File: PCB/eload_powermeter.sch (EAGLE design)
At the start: 66 parts, among them IC1 ADS1115_IC, IC2 AD826R, IC3 TP4056, IC4 FS312F-G, IC5 MT3608, K1 HJR-4102E, K2 TXD2SA-4.5V, Q1 BSS123, Q2 YSX321SL20H, Q3 BSS123, Q4 IRF520, Q5 BSS123, SW1 ENCODER, U1 ATMEGA328P-AU

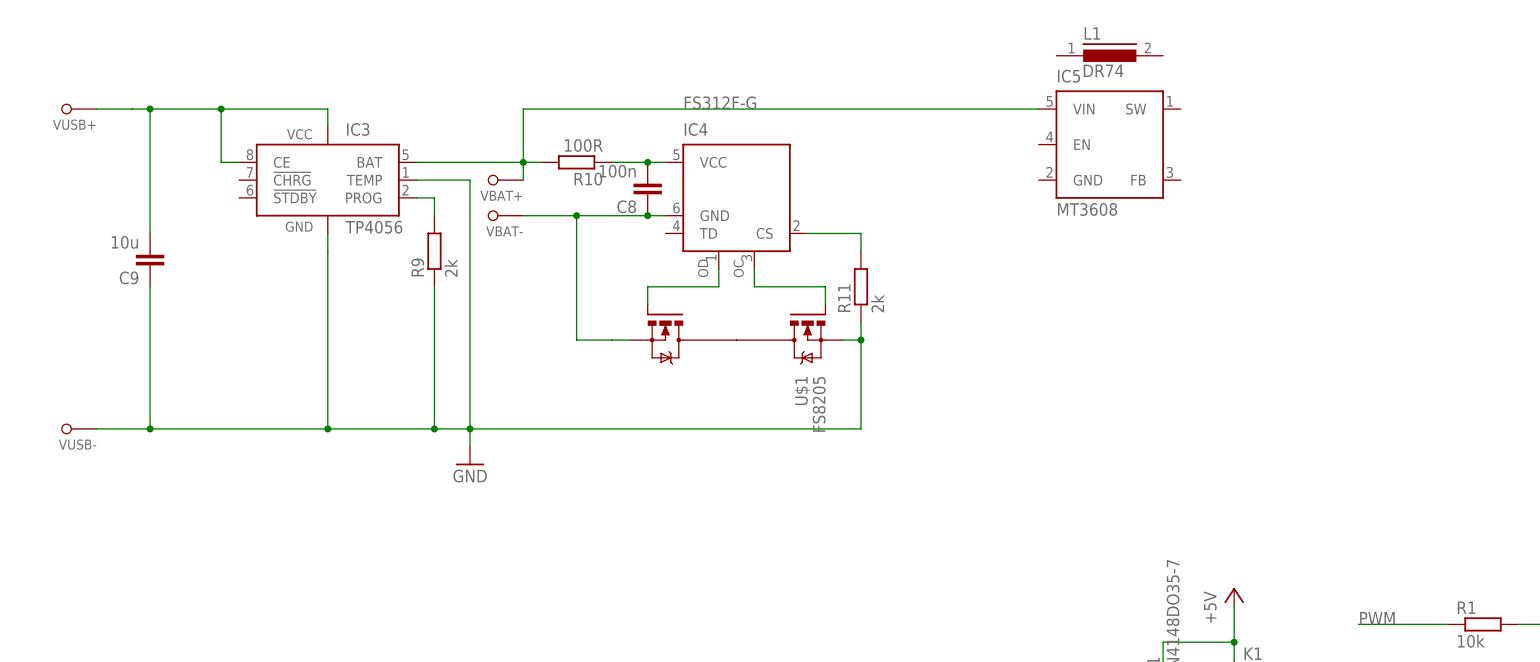
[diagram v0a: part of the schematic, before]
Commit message: finish boost circuit, start reverse surface mount led
Finishing the boost converter circuit and selecting the inductor and the schottky diode.
Starting with the footprint of the reverse surface mount led.
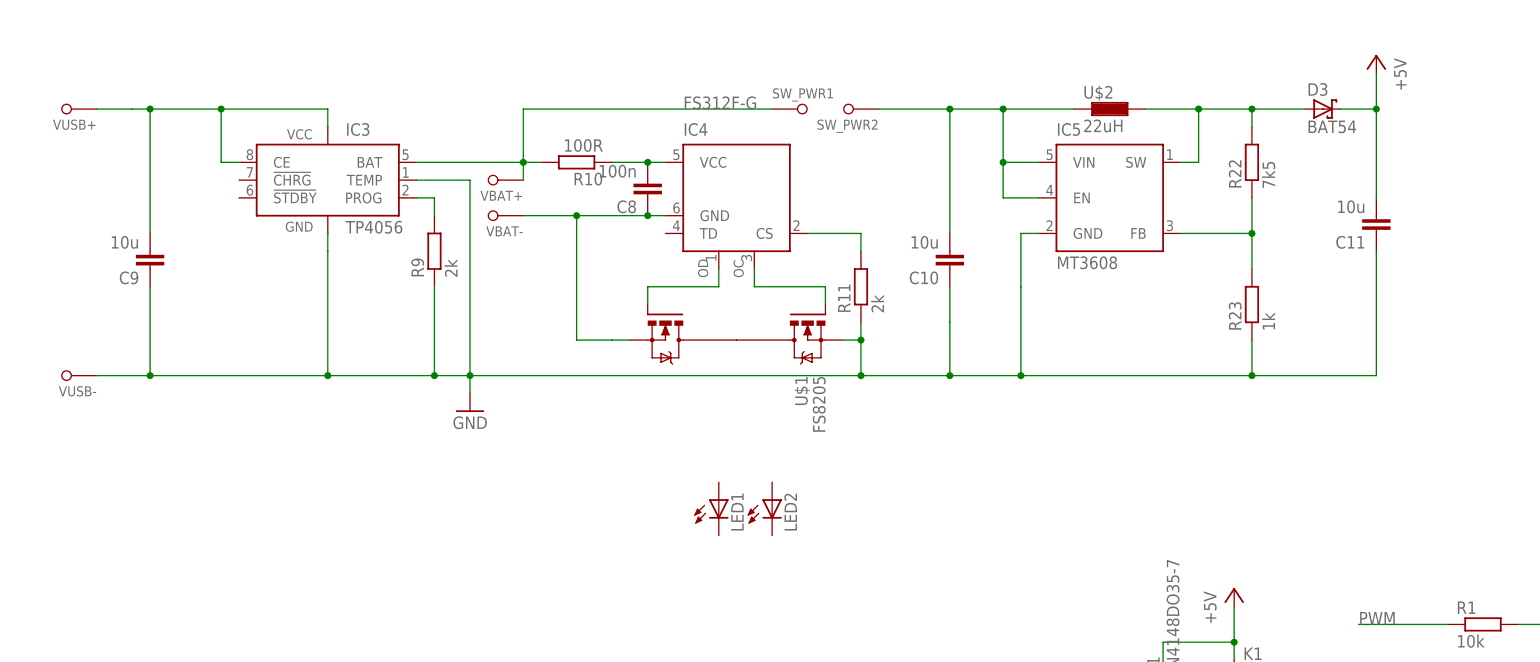
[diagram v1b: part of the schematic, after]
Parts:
- removed L1: DR74, inductors:DR74
- added C10, C11: 10u, rcl:C-EUC0603
- added D3: BAT54, diode:BAT54
- added LED1: (no value), led:LEDCHIPLED_1206
- added LED2: (no value), led:LEDCHIPLED_0805
- added R22: 7k5, rcl:R-EU_R0603
- added R23: 1k, rcl:R-EU_R0603
- added SW_PWR1, SW_PWR2: SOLDER_PAD, eload_powermeter:SOLDER_PAD
- added U$2: 22uH, eload_powermeter:L_1210
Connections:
- new net N$19: D3.A, IC5.SW, R22.2, U$2.2
- new net N$25: IC5.FB, R22.1, R23.2
- new net N$26: IC3.BAT, R10.2, SW_PWR1.P$1, VBAT+.P$1
- net +5V: now also C11.2, D3.C
- net GND: now also C10.1, C11.1, IC5.GND, R23.1
- net N$23: now also C10.2, IC5.EN, SW_PWR2.P$1, U$2.1; no longer IC3.BAT, R10.2, VBAT+.P$1
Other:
- moved on the sheet: IC5, VUSB-

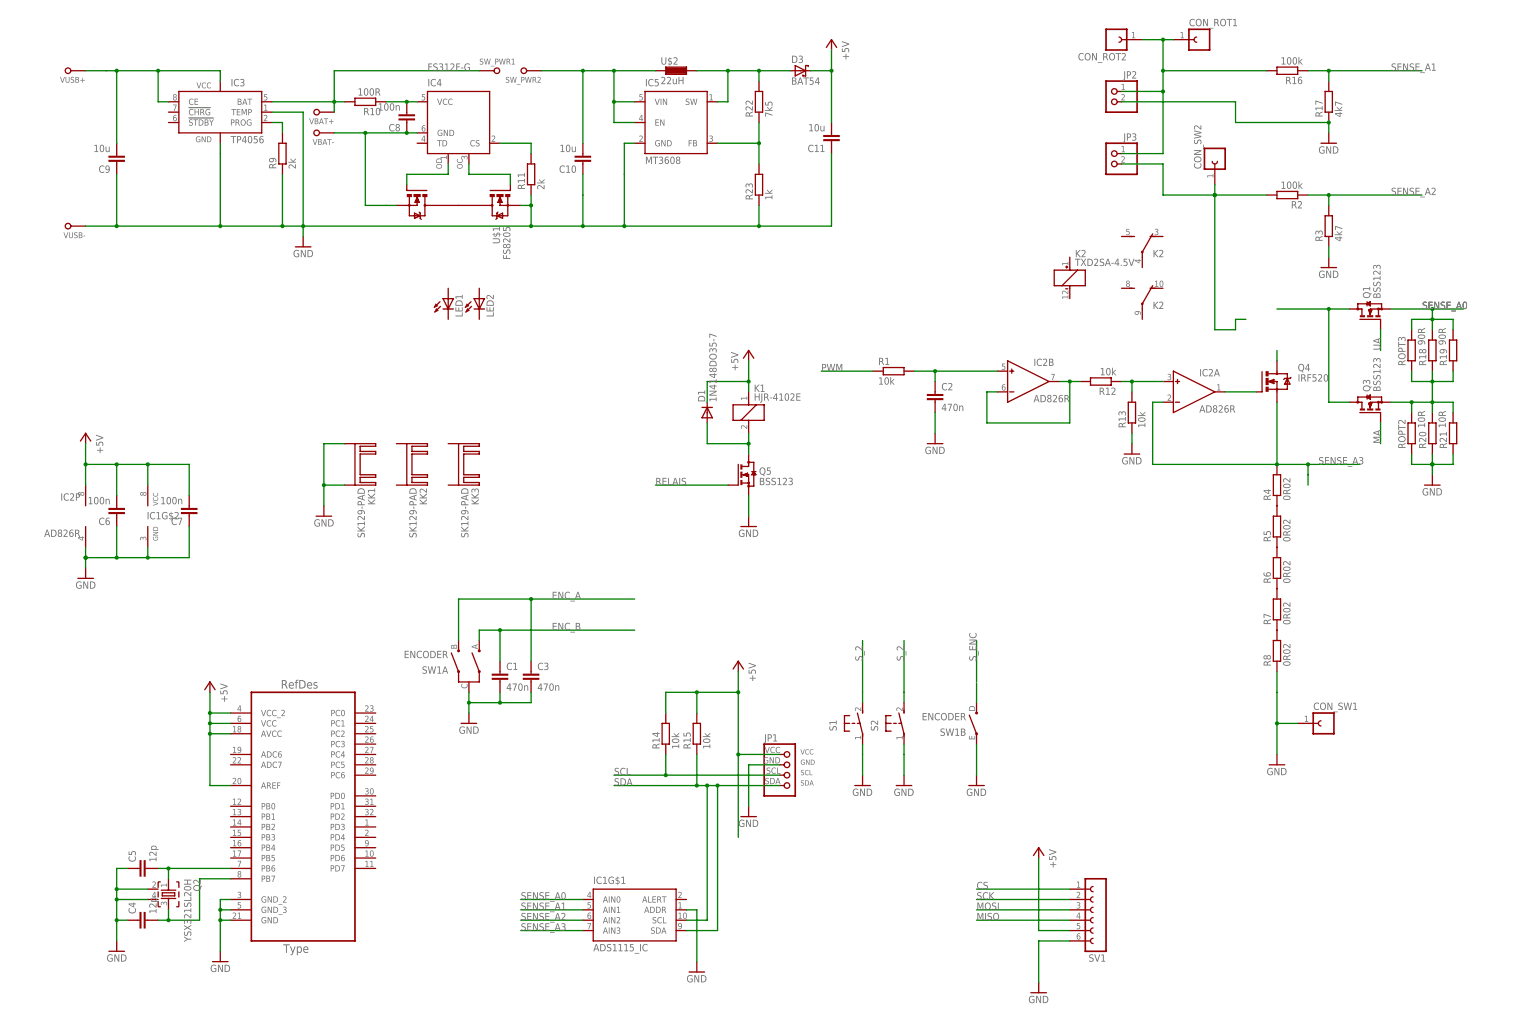
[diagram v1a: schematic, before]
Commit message: Current Sense Schematic, Switching a few components
Working on the current sense schematic. Cleaning up some other parts. Switching a few components/footprints - primariliy the footprint of the oled screen.
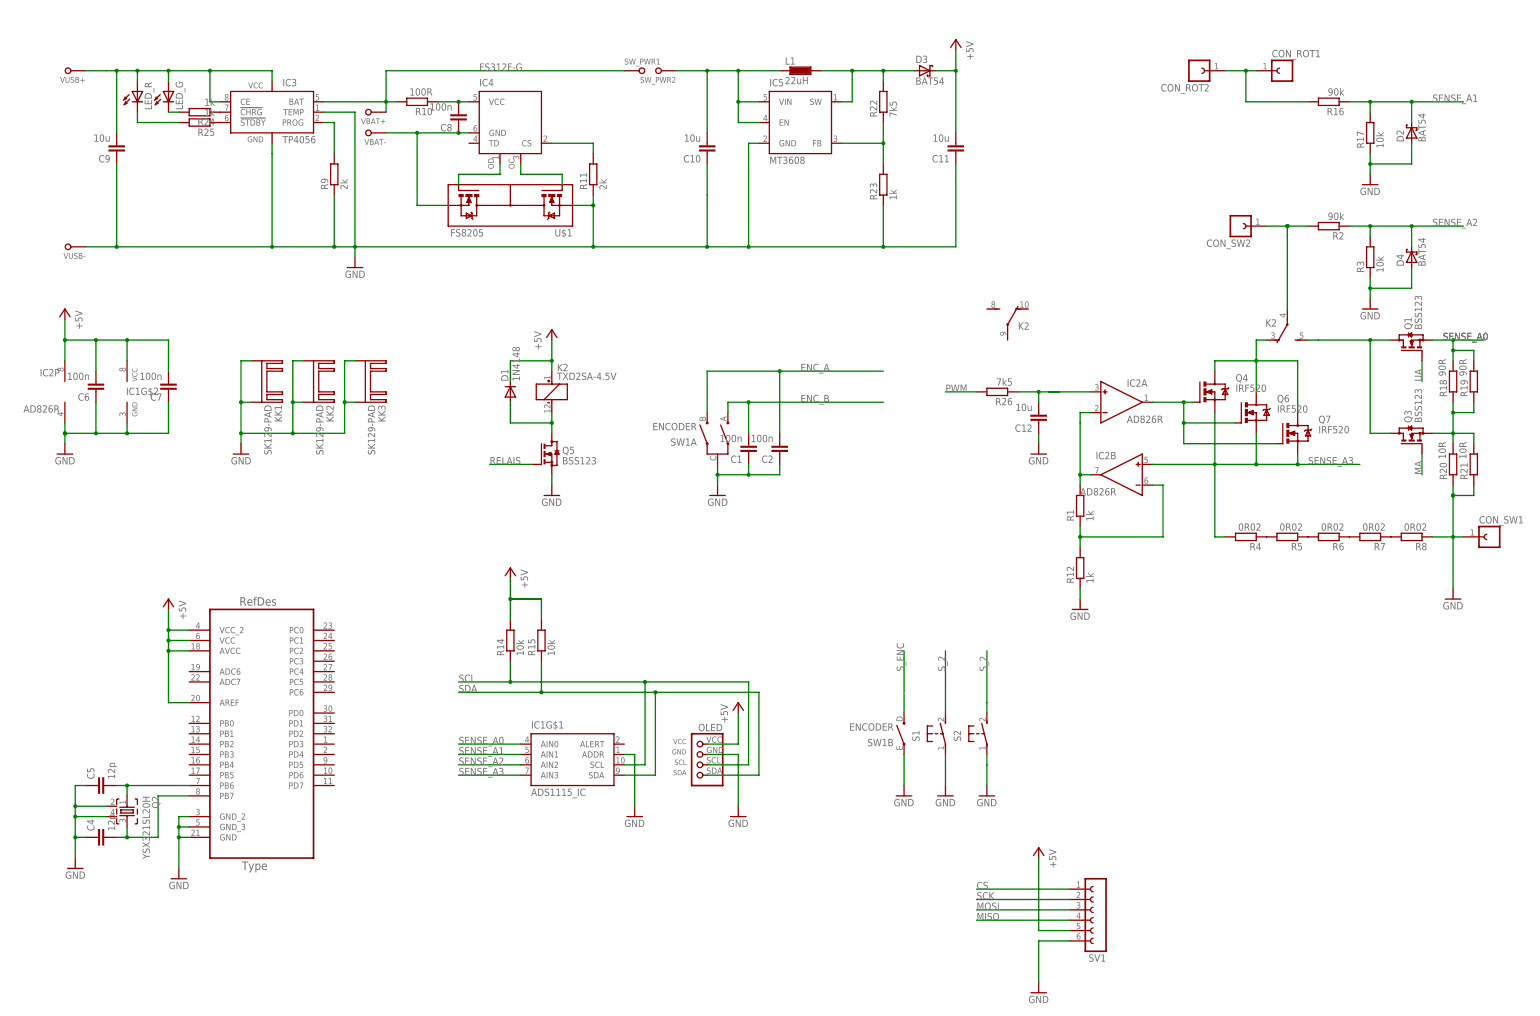
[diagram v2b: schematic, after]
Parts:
- removed C3: 470n, rcl:C-EUC1206K
- removed JP1: (no value), PowerMeter:OLED_128X32
- removed JP2, JP3: (no value), pinhead:PINHD-1X2
- removed K1: HJR-4102E, PowerMeter:HJR-4102E
- removed LED1: (no value), led:LEDCHIPLED_1206
- removed LED2: (no value), led:LEDCHIPLED_0805
- removed R13: 10k, rcl:R-EU_M1206
- removed ROPT2, ROPT3: (no value), PowerMeter:R-EU_OWN0207/10
- removed U$2: 22uH, eload_powermeter:L_1210
- added C12: 10u, rcl:C-EUC0603
- added D2, D4: BAT54, diode:BAT54
- added L1: 22uH, eload_powermeter:L_1210
- added LED_G, LED_R: (no value), eload_powermeter:LED_REVERSE_MOUNTSMT1206_REVERSE
- added OLED: (no value), eload_powermeter:OLED_128X32
- added Q6, Q7: IRF520, transistor-power:IRF520
- added R24, R25: 1k, rcl:R-EU_R0603
- added R26: 7k5, rcl:R-EU_R0603
- C1, C2: value 470n -> 100n; device rcl:C-EUC1206K -> rcl:C-EUC0603
- D1: value 1N4148DO35-7 -> 1N4148; device diode:1N4148DO35-7 -> diode:MBR0520LT
- R1, R12: value 10k -> 1k; device rcl:R-EU_M1206 -> rcl:R-EU_R0603
- R14, R15, R18, R19, R20, R21: device rcl:R-EU_M1206 -> rcl:R-EU_R0603
- R16, R2: value 100k -> 90k; device rcl:R-EU_M1206 -> rcl:R-EU_R0603
- R17, R3: value 4k7 -> 10k; device rcl:R-EU_M1206 -> rcl:R-EU_R0603
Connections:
- removed net N$13: CON_SW2.9, JP3.2, R2.2
- new net N$27: IC3.!CHRG, R24.1
- new net N$28: IC3.!STDBY, R25.1
- new net N$29: LED_G.C, R24.2
- new net N$30: LED_R.C, R25.2
- new net N$33: IC2B.IN-, R1.1, R12.2
- net +5V: now also K2_.+, OLED.VDD; no longer JP1.VDD, K11.1
- net ENC_A: now also C2.2; no longer C3.1
- net ENC_B: now also C1.2; no longer C1.1
- net GND: now also C1.1, C12.1, C2.1, D2.A, D4.A, KK2.K@1, KK2.K@2, KK3.K@1, KK3.K@2, OLED.GND, R12.1; no longer C1.2, C2.2, C3.2, JP1.GND, JP2.2, R13.1, ROPT2.1
- net N$1: no longer JP2.1, JP3.1
- net N$10: now also K2_.-; no longer K11.2
- net N$14: now also CON_SW2.9, K2G$1.P, R2.2; no longer Q4.D
- net N$19: now also L1.2; no longer U$2.2
- net N$2: now also Q6.G, Q7.G
- net N$23: now also L1.1; no longer U$2.1
- net N$3: no longer ROPT2.2, ROPT3.1
- net N$5: now also K2G$1.S
- net N$7: now also IC2A.IN-, R1.2; no longer IC2B.IN-, R12.2
- net N$8: now also C12.2, IC2A.IN+, R26.1; no longer C2.1, IC2B.IN+, R1.2
- net N$9: now also K2G$1.O, Q4.D, Q6.D, Q7.D; no longer IC2A.IN+, R12.1, R13.2
- net PWM: now also R26.2; no longer R1.1
- net SCL: now also IC1G$1.SCL, OLED.SCL; no longer JP1.SCL
- net SDA: now also OLED.SDA; no longer IC1G$1.SCL, JP1.SDA
- net SENSE_A0: no longer ROPT3.2
- net SENSE_A1: now also D2.C
- net SENSE_A2: now also D4.C
- net SENSE_A3: now also IC2B.IN+, Q6.S, Q7.S; no longer IC2A.IN-
- net VCC: now also LED_G.A, LED_R.A
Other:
- moved on the sheet: C1, C10, C11, C2, C4, C5, C6, C7, C8, C9, CON_ROT1, CON_ROT2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

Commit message: Finishing Schematic, Starting with Layout
Finishing and cleaning up the schematic, but also replacing some components and optimizing some footprints, for example the ATmega.
Starting with the PCB Layout - placing the components, wiring up the power circuit and the power cuircuit.
Adding an excel file, which shows the data of the chosen values of the current shunt resistors.
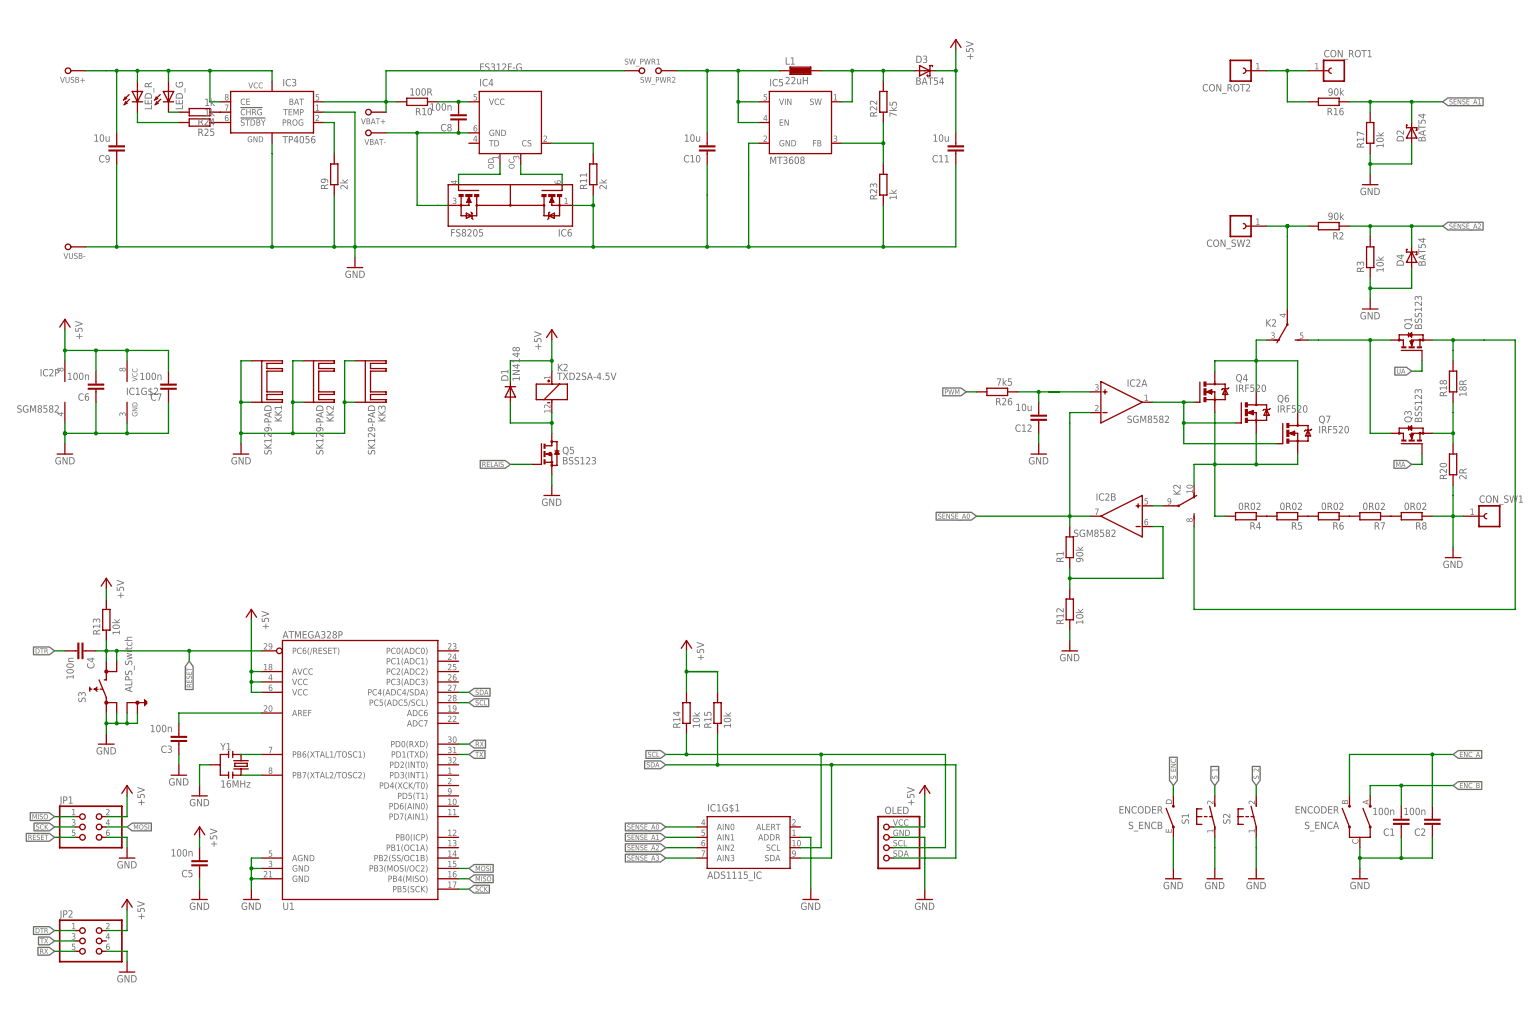
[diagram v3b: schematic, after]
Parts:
- removed Q2: YSX321SL20H, eload_powermeter:YSX321SL20H
- removed R19: 90R, rcl:R-EU_R0603
- removed R21: 10R, rcl:R-EU_R0603
- removed SV1: (no value), con-lsta:FE06-1
- removed SW1: ENCODER, eload_powermeter:ENCODER
- added C3: 100n, rcl:C-EUC0603
- added JP1, JP2: (no value), eload_powermeter:PINHD-2X3_SMD
- added R13: 10k, rcl:R-EU_R0603
- added S3: ALPS_Switch, eload_powermeter:ALPS_SKSGPAE010S
- added S_ENC: ENCODER, eload_powermeter:ENCODER
- added Y1: 16MHz, eload_powermeter:RESONATOR1:1
- C4, C5: value 12p -> 100n
- IC2: value AD826R -> SGM8582
- KK1, KK2, KK3: device heatsink:SK129-PAD -> eload_powermeter:SK129-PAD
- R1: value 1k -> 90k
- R12: value 1k -> 10k
- R18: value 90R -> 18R
- R20: value 10R -> 2R
- U1: value ATMEGA328P-AU -> ATMEGA328P; device eload_powermeter:ATMEGA328P-AU -> eload_powermeter:ATMEGA328P
- renumbered U$1 to IC6
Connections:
- net N$26 renamed VBAT+
- removed net CS: SV1.1
- removed net VCC: C6.2, C7.2, C8.2, C9.2, IC1G$2.VCC, IC2P.V+, IC3.CE, IC3.VCC, IC4.VCC, LED_G.A, LED_R.A, R10.1, VUSB+.P$1
- new net DTR: C4.2, JP2.1
- new net N$13: IC2B.IN+, K2G$2.P
- new net N$31: C3.2, U1.AREF
- new net N$40: K2G$2.S, Q1.S, R18.2
- new net RESET: C4.1, JP1.5, R13.1, S3.4.1, S3.4.2, U1.PC6(/RESET)
- new net RX: JP2.5, U1.PD0(RXD)
- new net S_1: S1.S
- new net S_ENC: S_ENCB.D
- new net TX: JP2.3, U1.PD1(TXD)
- new net VBAT-: C8.1, IC4.GND, IC6.S2, VBAT-.P$1
- new net VUSB: C9.2, IC3.CE, IC3.VCC, LED_G.A, LED_R.A, VUSB+.P$1
- net +5V: now also C5.2, C6.2, C7.2, IC1G$2.VCC, IC2P.V+, JP1.2, JP2.2, R13.2, U1.VCC@1, U1.VCC@2; no longer SV1.5, U1.AREF, U1.VCC, U1.VCC_2
- net ENC_A: now also S_ENCA.B; no longer SW1A.B
- net ENC_B: now also S_ENCA.A; no longer SW1A.A
- net GND: now also C3.1, JP1.6, JP2.6, S3.3.1, S3.3.2, S3.SH1, S3.SH2, S_ENCA.C, S_ENCB.E, U1.AGND, U1.GND@1, U1.GND@2, Y1.2; no longer C4.1, C8.1, IC4.GND, IC6.S2, Q2.2, Q2.4, R21.1, SV1.6, SW1A.C, SW1B.E, U1.GND, U1.GND_2, U1.GND_3, VBAT-.P$1
- net MISO: now also JP1.1, U1.PB4(MISO); no longer SV1.4
- net MOSI: now also JP1.4, U1.PB3(MOSI/OC2); no longer SV1.3
- net N$12: now also U1.PB6(XTAL1/TOSC1), Y1.1; no longer C5.2, Q2.1, U1.PB6
- net N$15: now also U1.PB7(XTAL2/TOSC2), Y1.3; no longer C4.2, Q2.3, U1.PB7
- net N$16: now also C8.2, IC4.VCC, R10.1; no longer SW1B.D
- net N$3: no longer R19.1, R21.2
- net N$7: now also K2G$2.O, Q4.S, Q6.S, Q7.S, R4.2; no longer IC2A.IN-, IC2B.OUT, R1.2
- net SCK: now also JP1.3, U1.PB5(SCK); no longer SV1.2
- net SCL: now also U1.PC5(ADC5/SCL)
- net SDA: now also U1.PC4(ADC4/SDA)
- net SENSE_A0: now also IC2A.IN-, IC2B.OUT, R1.2; no longer Q1.S, R18.2, R19.2
- net SENSE_A3: no longer IC2B.IN+, Q4.S, Q6.S, Q7.S, R4.2
- net S_2: no longer S1.S
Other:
- moved on the sheet: C1, C2, C4, C5, CON_ROT1, CON_ROT2, CON_SW1, IC1G$1, IC2B, K2, R1, R12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
